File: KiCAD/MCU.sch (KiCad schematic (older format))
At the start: 22 parts, among them J25 Conn_02x18_Odd_Even, J26 Conn_02x18_Odd_Even, J27 Conn_02x18_Odd_Even, J28 Conn_02x18_Odd_Even, U9 STM32F765ZITx

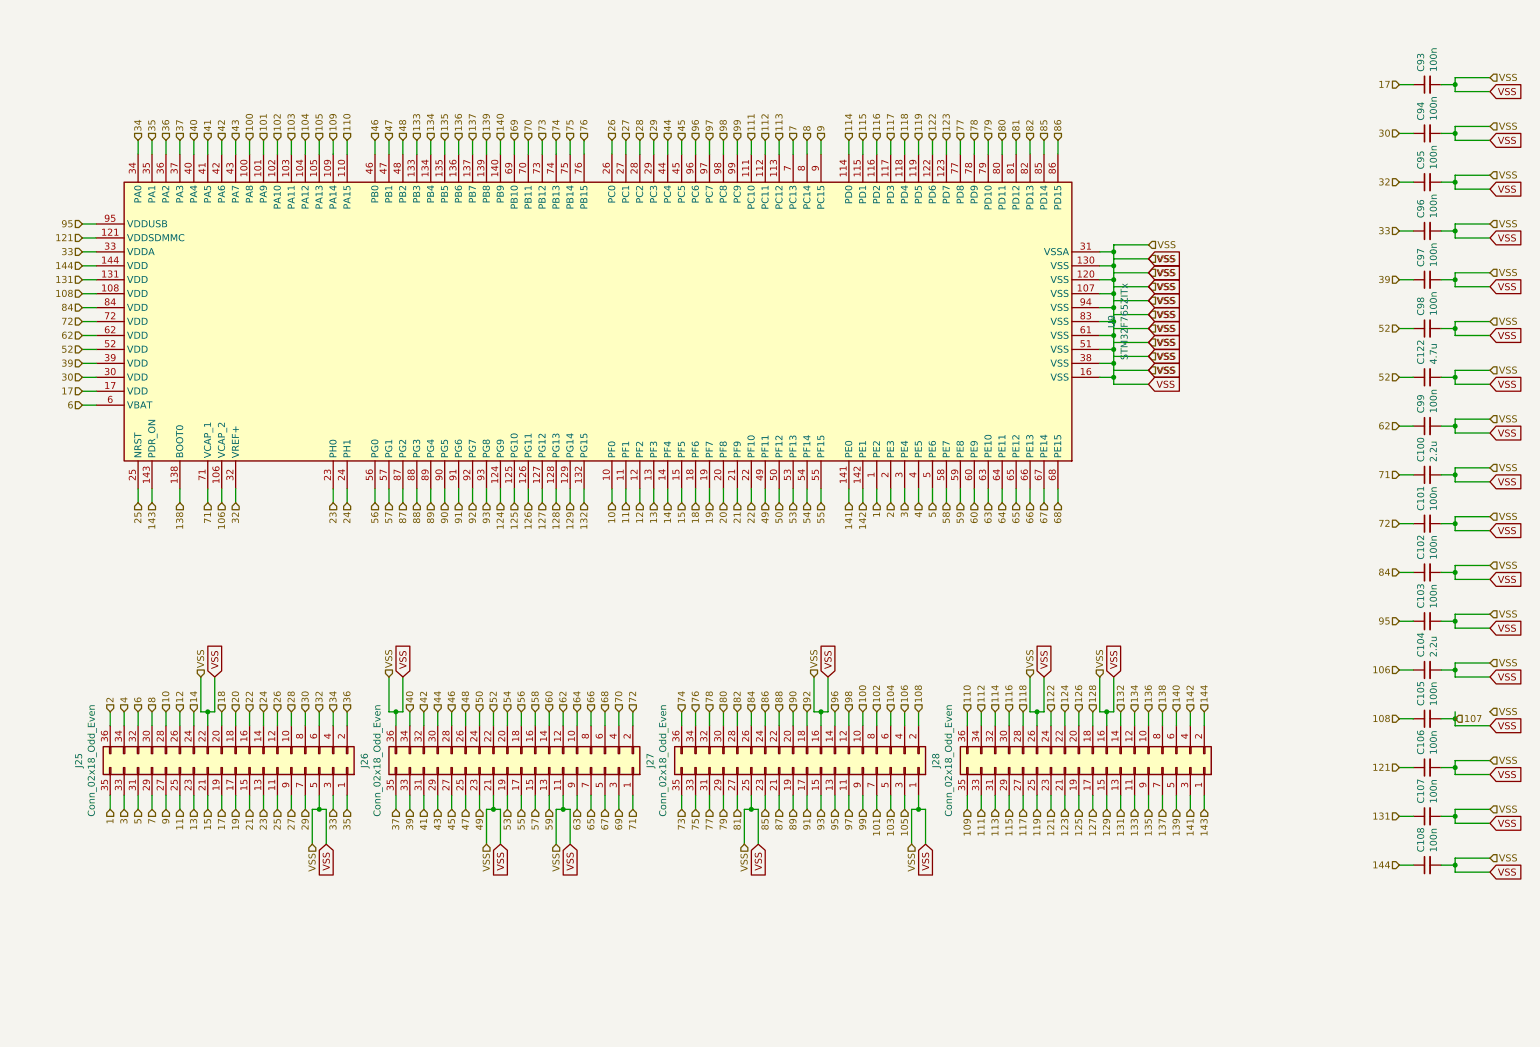
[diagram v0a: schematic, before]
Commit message: added usb, crystals
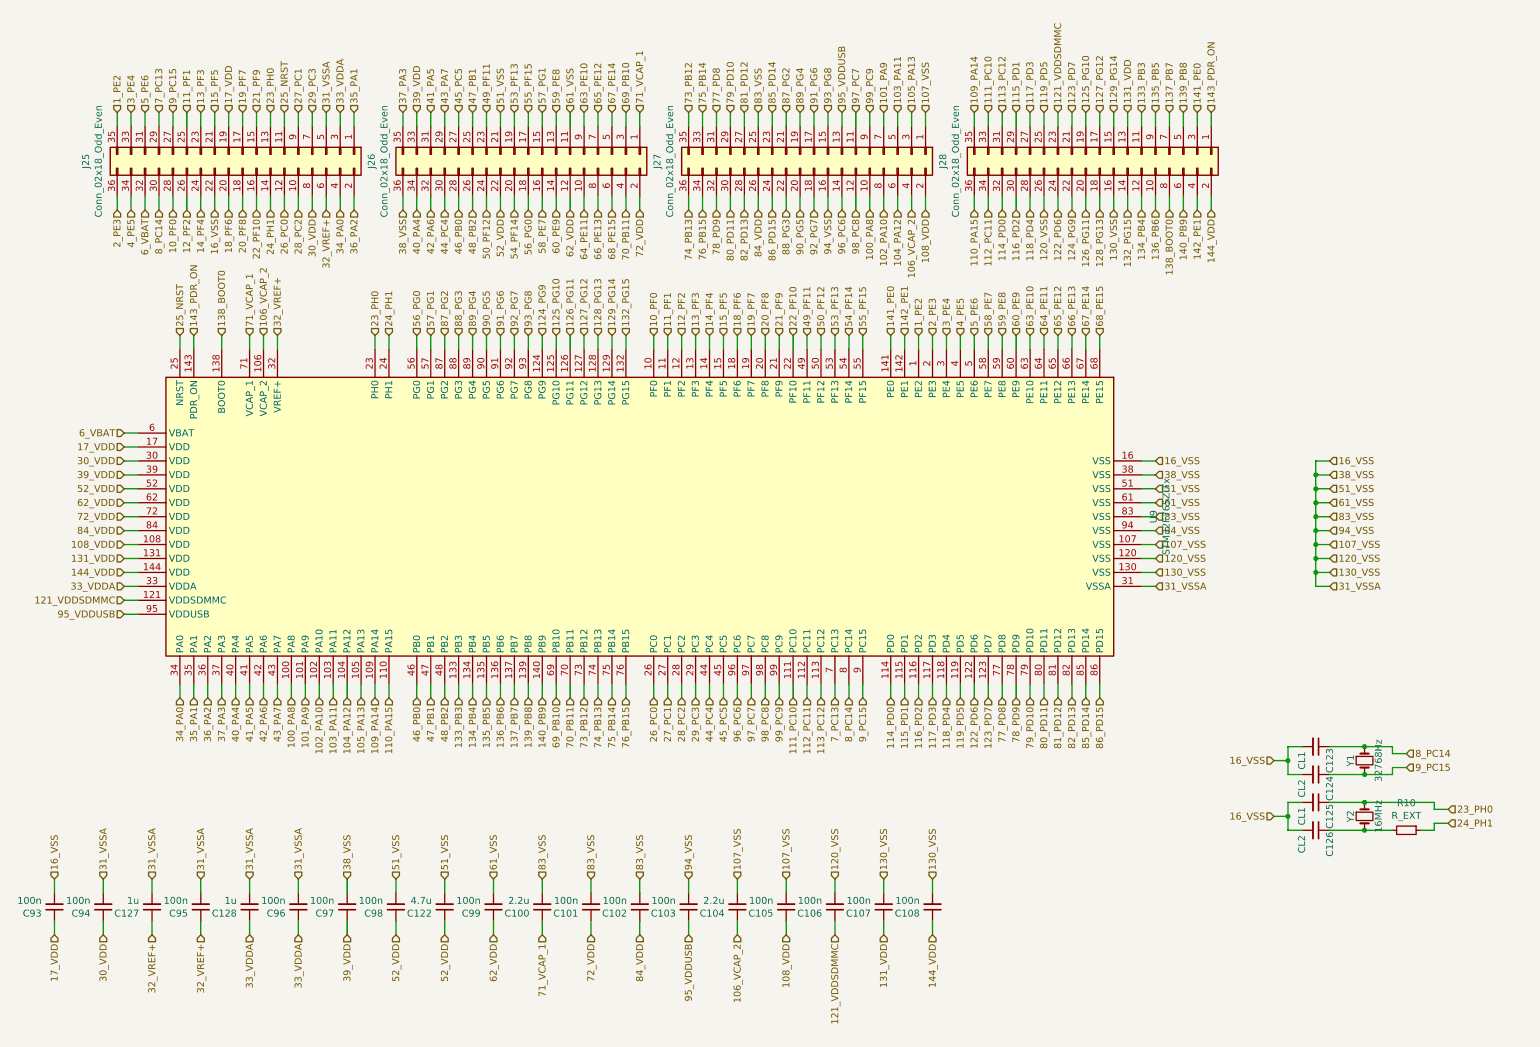
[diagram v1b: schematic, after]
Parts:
- added C123, C125: CL1, Capacitor_SMD:C_0402_1005Metric, symbol Device:C_Small
- added C124, C126: CL2, Capacitor_SMD:C_0402_1005Metric, symbol Device:C_Small
- added C127: 1u, Capacitor_SMD:C_0402_1005Metric, symbol Device:C_Small
- added C128: 1u, Capacitor_SMD:C_0603_1608Metric, symbol Device:C_Small
- added R10: R_EXT, Resistor_SMD:R_0402_1005Metric, symbol Device:R_Small
- added Y1: 32768Hz, Crystal:Crystal_SMD_MicroCrystal_CC4V-T1A-2Pin_5.0x1.9mm, symbol Device:Crystal_Small
- added Y2: 16MHz, Crystal:Crystal_SMD_5032-4Pin_5.0x3.2mm, symbol Device:Crystal_Small
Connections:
- net 1 renamed 1_PE2
- net 10 renamed 10_PF0
- net 100 renamed 100_PA8
- net 101 renamed 101_PA9
- net 102 renamed 102_PA10
- net 103 renamed 103_PA11
- net 104 renamed 104_PA12
- net 105 renamed 105_PA13
- net 106 renamed 106_VCAP_2
- net 108 renamed 108_VDD
- net 109 renamed 109_PA14
- net 11 renamed 11_PF1
- net 110 renamed 110_PA15
- net 111 renamed 111_PC10
- net 112 renamed 112_PC11
- net 113 renamed 113_PC12
- net 114 renamed 114_PD0
- net 115 renamed 115_PD1
- net 116 renamed 116_PD2
- net 117 renamed 117_PD3
- net 118 renamed 118_PD4
- net 119 renamed 119_PD5
- net 12 renamed 12_PF2
- net 121 renamed 121_VDDSDMMC
- net 122 renamed 122_PD6
- net 123 renamed 123_PD7
- net 124 renamed 124_PG9
- net 125 renamed 125_PG10
- net 126 renamed 126_PG11
- net 127 renamed 127_PG12
- net 128 renamed 128_PG13
- net 129 renamed 129_PG14
- net 13 renamed 13_PF3
- net 131 renamed 131_VDD
- net 132 renamed 132_PG15
- net 133 renamed 133_PB3
- net 134 renamed 134_PB4
- net 135 renamed 135_PB5
- net 136 renamed 136_PB6
- net 137 renamed 137_PB7
- net 138 renamed 138_BOOT0
- net 139 renamed 139_PB8
- net 14 renamed 14_PF4
- net 140 renamed 140_PB9
- net 141 renamed 141_PE0
- net 142 renamed 142_PE1
- net 143 renamed 143_PDR_ON
- net 144 renamed 144_VDD
- net 15 renamed 15_PF5
- net 17 renamed 17_VDD
- net 18 renamed 18_PF6
- net 19 renamed 19_PF7
- net 2 renamed 2_PE3
- net 20 renamed 20_PF8
- net 21 renamed 21_PF9
- net 22 renamed 22_PF10
- net 23 renamed 23_PH0
- net 23_PH0: now also C125.1, Y2.1
- net 24 renamed 24_PH1
- net 24_PH1: now also R10.1
- net 25 renamed 25_NRST
- net 26 renamed 26_PC0
- net 27 renamed 27_PC1
- net 28 renamed 28_PC2
- net 29 renamed 29_PC3
- net 3 renamed 3_PE4
- net 30 renamed 30_VDD
- net 32 renamed 32_VREF+
- net 32_VREF+: now also C127.1
- net 33 renamed 33_VDDA
- net 33_VDDA: now also C128.1
- net 34 renamed 34_PA0
- net 35 renamed 35_PA1
- net 36 renamed 36_PA2
- net 37 renamed 37_PA3
- net 39 renamed 39_VDD
- net 4 renamed 4_PE5
- net 40 renamed 40_PA4
- net 41 renamed 41_PA5
- net 42 renamed 42_PA6
- net 43 renamed 43_PA7
- net 44 renamed 44_PC4
- net 45 renamed 45_PC5
- net 46 renamed 46_PB0
- net 47 renamed 47_PB1
- net 48 renamed 48_PB2
- net 49 renamed 49_PF11
- net 5 renamed 5_PE6
- net 50 renamed 50_PF12
- net 52 renamed 52_VDD
- net 53 renamed 53_PF13
- net 54 renamed 54_PF14
- net 55 renamed 55_PF15
- net 56 renamed 56_PG0
- net 57 renamed 57_PG1
- net 58 renamed 58_PE7
- net 59 renamed 59_PE8
- net 6 renamed 6_VBAT
- net 60 renamed 60_PE9
- net 62 renamed 62_VDD
- net 63 renamed 63_PE10
- net 64 renamed 64_PE11
- net 65 renamed 65_PE12
- net 66 renamed 66_PE13
- net 67 renamed 67_PE14
- net 68 renamed 68_PE15
- net 69 renamed 69_PB10
- net 7 renamed 7_PC13
- net 70 renamed 70_PB11
- net 71 renamed 71_VCAP_1
- net 72 renamed 72_VDD
- net 73 renamed 73_PB12
- net 74 renamed 74_PB13
- net 75 renamed 75_PB14
- net 76 renamed 76_PB15
- net 77 renamed 77_PD8
- net 78 renamed 78_PD9
- net 79 renamed 79_PD10
- net 8 renamed 8_PC14
- net 8_PC14: now also C123.1, Y1.1
- net 80 renamed 80_PD11
- net 81 renamed 81_PD12
- net 82 renamed 82_PD13
- net 84 renamed 84_VDD
- net 85 renamed 85_PD14
- net 86 renamed 86_PD15
- net 87 renamed 87_PG2
- net 88 renamed 88_PG3
- net 89 renamed 89_PG4
- net 9 renamed 9_PC15
- net 9_PC15: now also C124.1, Y1.2
- net 90 renamed 90_PG5
- net 91 renamed 91_PG6
- net 92 renamed 92_PG7
- net 93 renamed 93_PG8
- net 95 renamed 95_VDDUSB
- net 96 renamed 96_PC6
- net 97 renamed 97_PC7
- net 98 renamed 98_PC8
- net 99 renamed 99_PC9
- net VSS renamed 107_VSS
- net 107_VSS: now also C123.2, C124.2, C125.2, C126.2, C127.2, C128.2
- new net: C126.1, R10.2, Y2.2
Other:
- moved on the sheet: C100, C101, C102, C103, C104, C105, C106, C107, C108, C122, C93, C94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
